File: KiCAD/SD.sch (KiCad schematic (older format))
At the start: 3 parts, among them J37 Conn_01x05, J38 Conn_01x04, U13 473521001

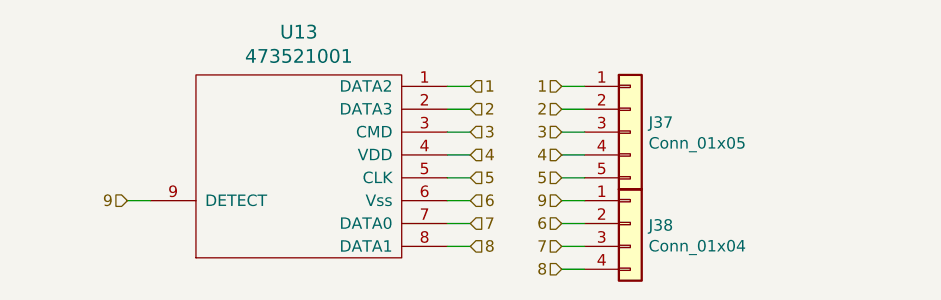
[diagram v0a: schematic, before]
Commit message: added usb, crystals
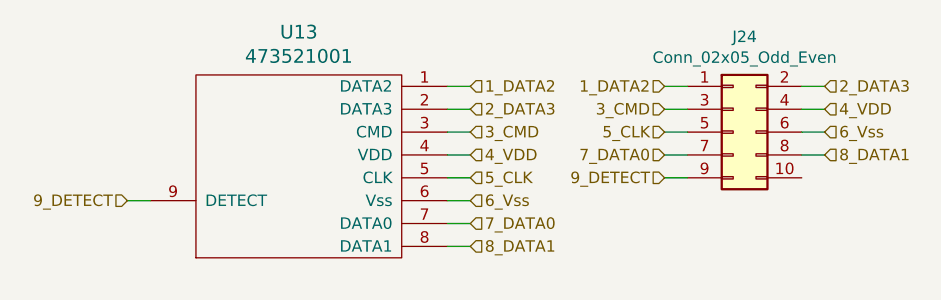
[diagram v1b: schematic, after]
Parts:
- removed J37: Conn_01x05, Connector_PinHeader_2.54mm:PinHeader_1x05_P2.54mm_Vertical, symbol Connector_Generic:Conn_01x05
- removed J38: Conn_01x04, Connector_PinHeader_2.54mm:PinHeader_1x04_P2.54mm_Vertical, symbol Connector_Generic:Conn_01x04
- added J24: Conn_02x05_Odd_Even, Connector_PinHeader_2.54mm:PinHeader_2x05_P2.54mm_Vertical, symbol Connector_Generic:Conn_02x05_Odd_Even
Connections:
- net 1 renamed 1_DATA2
- net 1_DATA2: now also J24.1 (Pin_1)
- net 2 renamed 2_DATA3
- net 2_DATA3: now also J24.2 (Pin_2)
- net 3 renamed 3_CMD
- net 3_CMD: now also J24.3 (Pin_3)
- net 4 renamed 4_VDD
- net 4_VDD: now also J24.4 (Pin_4)
- net 5 renamed 5_CLK
- net 5_CLK: now also J24.5 (Pin_5)
- net 6 renamed 6_Vss
- net 6_Vss: now also J24.6 (Pin_6)
- net 7 renamed 7_DATA0
- net 7_DATA0: now also J24.7 (Pin_7)
- net 8 renamed 8_DATA1
- net 8_DATA1: now also J24.8 (Pin_8)
- net 9 renamed 9_DETECT
- net 9_DETECT: now also J24.9 (Pin_9)
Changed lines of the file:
@@
 $Descr A4 11693 8268
 encoding utf-8
-Sheet 14 17
+Sheet 14 18
 Title ""
 Date ""
@@
 	0    -1   -1   0
 $EndComp
-$Comp
-L Connector_Generic:Conn_01x04 J38
-U 1 1 5CDD444F
-P 7300 3600
-F 0 "J38" H 7380 3592 50  0000 L CNN
-F 1 "Conn_01x04" H 7380 3501 50  0000 L CNN
-F 2 "Connector_PinHeader_2.54mm:PinHeader_1x04_P2.54mm_Vertical" H 7300 3600 50  0001 C CNN
-F 3 "~" H 7300 3600 50  0001 C CNN
-	1    7300 3600
-	1    0    0    -1
-$EndComp
-$Comp
-L Connector_Generic:Conn_01x05 J37
-U 1 1 5CDD4496
-P 7300 3200
-F 0 "J37" H 7380 3242 50  0000 L CNN
-F 1 "Conn_01x05" H 7380 3151 50  0000 L CNN
-F 2 "Connector_PinHeader_2.54mm:PinHeader_1x05_P2.54mm_Vertical" H 7300 3200 50  0001 C CNN
-F 3 "~" H 7300 3200 50  0001 C CNN
-	1    7300 3200
-	1    0    0    -1
-$EndComp
-Text HLabel 7000 3000 0    50   Input ~ 0
-1
+Text HLabel 7450 3000 0    50   Input ~ 0
+1_DATA2
 Wire Wire Line
-	7000 3000 7100 3000
-Text HLabel 7000 3100 0    50   Input ~ 0
-2
+	7450 3000 7550 3000
+Text HLabel 8150 3000 2    50   Input ~ 0
+2_DATA3
 Wire Wire Line
-	7000 3100 7100 3100
-Text HLabel 7000 3200 0    50   Input ~ 0
-3
+	8150 3000 8050 3000
+Text HLabel 7450 3100 0    50   Input ~ 0
+3_CMD
 Wire Wire Line
-	7000 3200 7100 3200
-Text HLabel 7000 3300 0    50   Input ~ 0
-4
+	7450 3100 7550 3100
+Text HLabel 8150 3100 2    50   Input ~ 0
+4_VDD
 Wire Wire Line
-	7000 3300 7100 3300
-Text HLabel 7000 3600 0    50   Input ~ 0
-6
+	8150 3100 8050 3100
+Text HLabel 8150 3200 2    50   Input ~ 0
+6_Vss
 Wire Wire Line
-	7000 3600 7100 3600
-Text HLabel 7000 3800 0    50   Input ~ 0
-8
+	8150 3200 8050 3200
+Text HLabel 8150 3300 2    50   Input ~ 0
+8_DATA1
 Wire Wire Line
-	7000 3800 7100 3800
-Text HLabel 7000 3500 0    50   Input ~ 0
-9
+	8150 3300 8050 3300
+Text HLabel 7450 3400 0    50   Input ~ 0
+9_DETECT
 Wire Wire Line
-	7000 3500 7100 3500
+	7450 3400 7550 3400
 Wire Wire Line
-	7000 3700 7100 3700
+	7450 3300 7550 3300
 Wire Wire Line
-	7000 3400 7100 3400
-Text HLabel 7000 3400 0    50   Input ~ 0
-5
-Text HLabel 7000 3700 0    50   Input ~ 0
-7
+	7450 3200 7550 3200
+Text HLabel 7450 3200 0    50   Input ~ 0
+5_CLK
+Text HLabel 7450 3300 0    50   Input ~ 0
+7_DATA0
 Text HLabel 6600 3000 2    50   Input ~ 0
-1
+1_DATA2
 Wire Wire Line
 	6600 3000 6500 3000
 Text HLabel 6600 3100 2    50   Input ~ 0
-2
+2_DATA3
 Wire Wire Line
 	6600 3100 6500 3100
 Text HLabel 6600 3200 2    50   Input ~ 0
-3
+3_CMD
 Wire Wire Line
 	6600 3200 6500 3200
 Text HLabel 6600 3300 2    50   Input ~ 0
-4
+4_VDD
 Wire Wire Line
 	6600 3300 6500 3300
 Text HLabel 6600 3500 2    50   Input ~ 0
-6
+6_Vss
 Wire Wire Line
 	6600 3500 6500 3500
 Text HLabel 6600 3700 2    50   Input ~ 0
-8
+8_DATA1
 Wire Wire Line
 	6600 3700 6500 3700
 Text HLabel 5100 3500 0    50   Input ~ 0
-9
+9_DETECT
 Wire Wire Line
 	5100 3500 5200 3500
@@
 	6600 3400 6500 3400
 Text HLabel 6600 3400 2    50   Input ~ 0
-5
+5_CLK
 Text HLabel 6600 3600 2    50   Input ~ 0
-7
+7_DATA0
+$Comp
+L Connector_Generic:Conn_02x05_Odd_Even J24
+U 1 1 5CF51553
+P 7750 3200
+F 0 "J24" H 7800 3617 50  0000 C CNN
+F 1 "Conn_02x05_Odd_Even" H 7800 3526 50  0000 C CNN
+F 2 "Connector_PinHeader_2.54mm:PinHeader_2x05_P2.54mm_Vertical" H 7750 3200 50  0001 C CNN
+F 3 "~" H 7750 3200 50  0001 C CNN
+	1    7750 3200
+	1    0    0    -1
+$EndComp
 $EndSCHEMATC
